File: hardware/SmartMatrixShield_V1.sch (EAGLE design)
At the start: 10 parts, among them J1 CON_HEADER_2X08-PTH-SHROUDED, J4 1X2-5.0

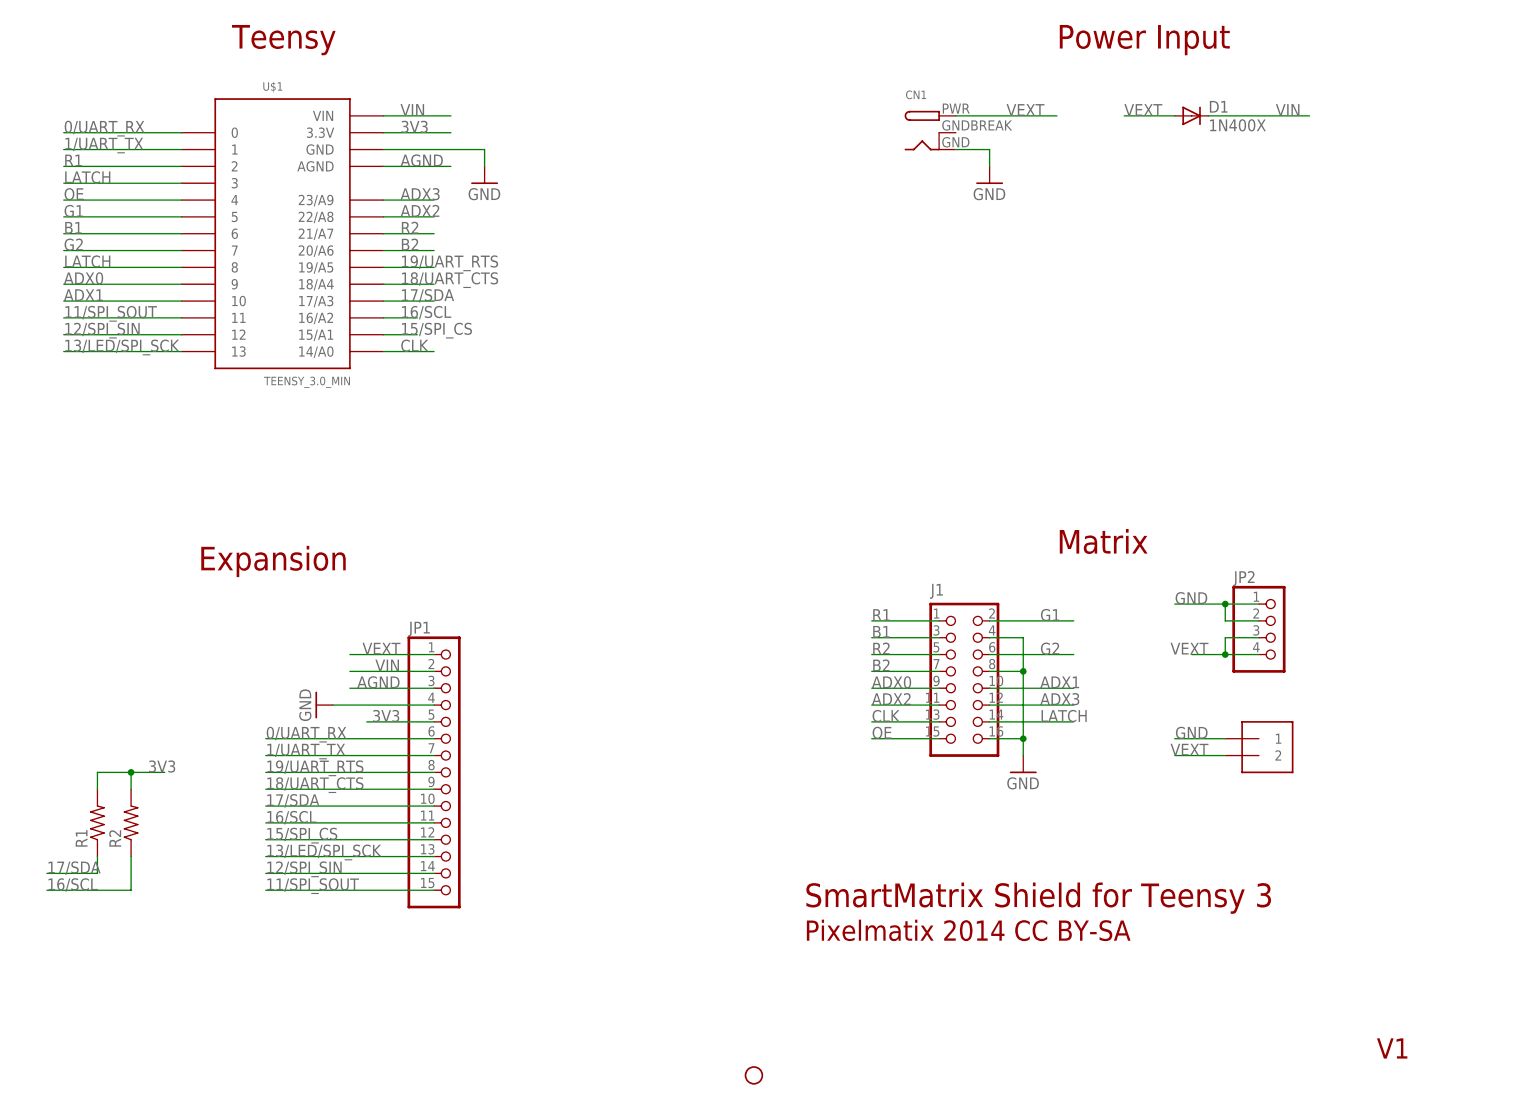
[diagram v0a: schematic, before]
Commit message: Schematic cleanup: Added some clarifying text
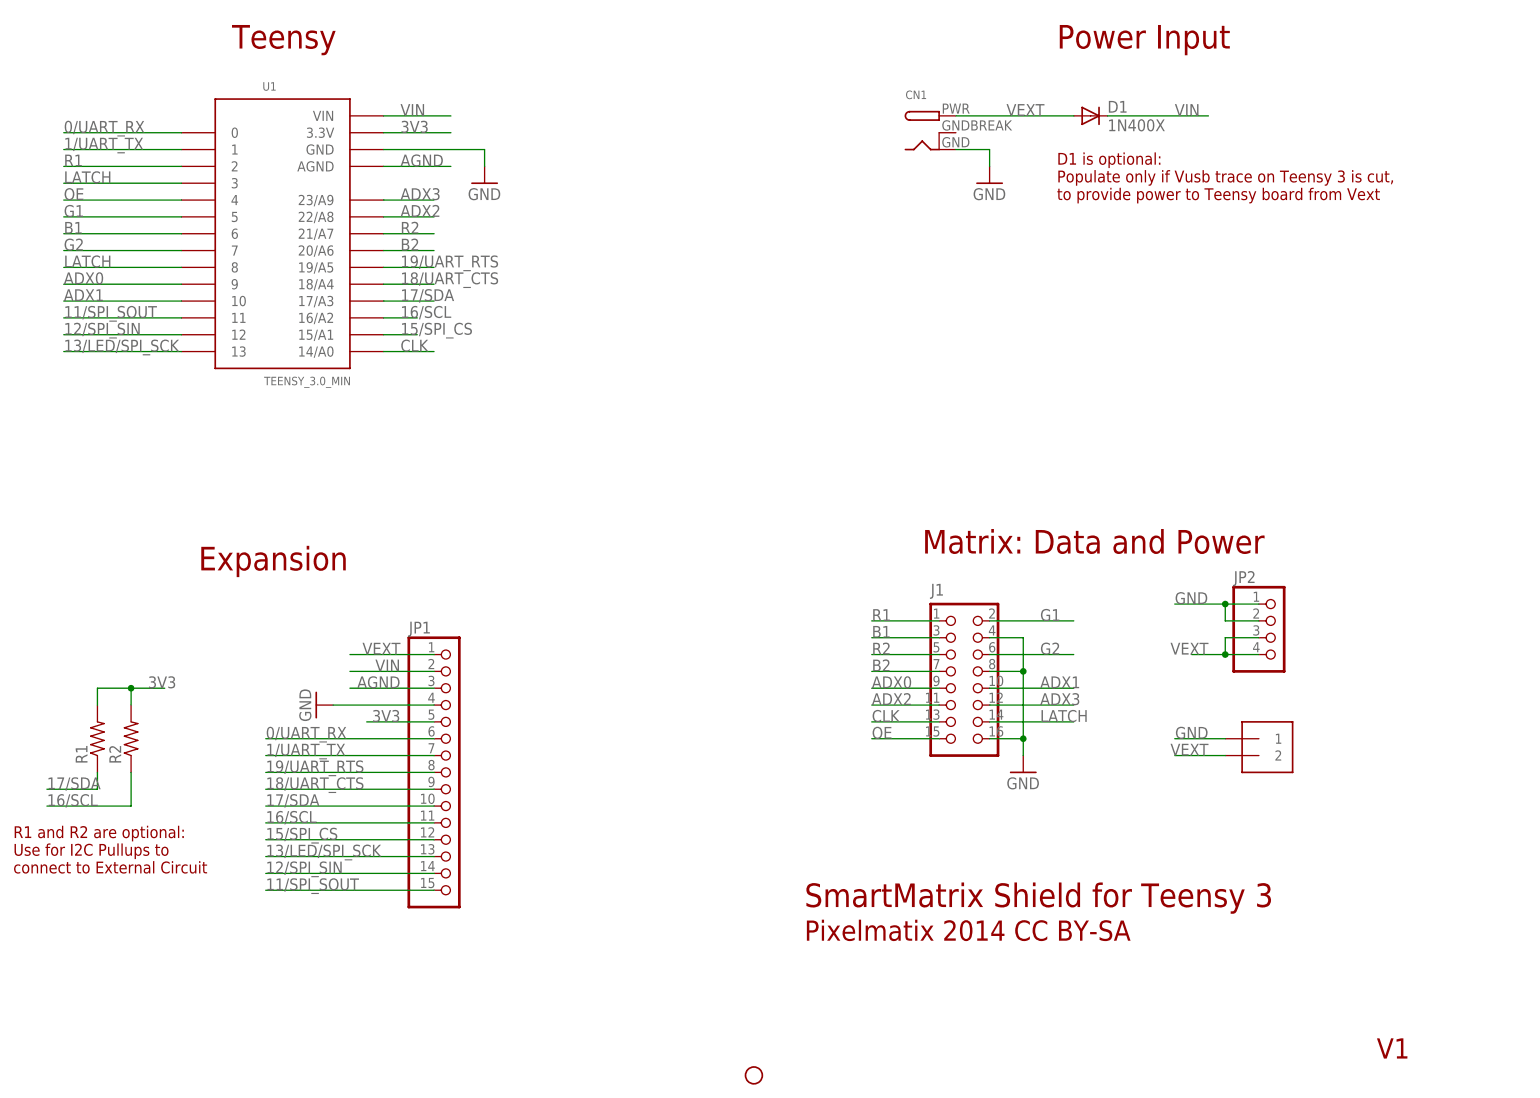
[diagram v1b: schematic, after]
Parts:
- renumbered U$1 to U1
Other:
- note added: "D1 is optional: Populate only if Vusb trace on Teensy 3 is cut, to provide power to Teensy board from Vext"
- note added: "Matrix: Data and Power"
- note added: "R1 and R2 are optional: Use for I2C Pullups to connect to External Circuit"
- note removed: "Matrix"
- moved on the sheet: D1, R1, R2
